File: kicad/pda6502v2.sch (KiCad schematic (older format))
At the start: 4 parts, among them U1 W65C02SxP, U2 AS6C62256-55PCN, U3 W65C22SxP, U4 AS6C62256-55PCN

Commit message: Lots of progress on schematic, some PCB part placement.
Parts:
- removed U3: W65C22SxP, Package_DIP:DIP-40_W15.24mm, symbol 65xx:W65C22SxP
- added C1, C10, C11, C14, C15, C16, C17, C2, C22, C23, C24, C3, C4, C5, C6, C7, C8, C9: 0.1μF, Capacitor_SMD:C_0805_2012Metric_Pad1.18x1.45mm_HandSolder, symbol Device:C_Small
- added C12: 100uF, Capacitor_THT:CP_Radial_D5.0mm_P2.00mm, symbol Device:CP
- added C13: 10uF, Capacitor_THT:CP_Radial_D5.0mm_P2.00mm, symbol Device:CP
- added C18, C19: 10nF, Capacitor_SMD:C_0805_2012Metric_Pad1.18x1.45mm_HandSolder, symbol Device:C_Small
- added C20, C21: 10uF, Capacitor_SMD:C_0805_2012Metric_Pad1.18x1.45mm_HandSolder, symbol Device:C_Small
- added D1: 1N5819, Diode_THT:D_DO-41_SOD81_P10.16mm_Horizontal, symbol Diode:1N5819
- added D10, D3, D4, D5, D6, D7, D8, D9: LED, LED_SMD:LED_0805_2012Metric_Pad1.15x1.40mm_HandSolder, symbol Device:LED_Small
- added D2: LED, LED_THT:LED_D3.0mm, symbol Device:LED
- added D?: 1N4148W, Diode_SMD:D_SOD-123, symbol Diode:1N4148W
- added J1: GPIOA, Connector_PinHeader_2.54mm:PinHeader_2x07_P2.54mm_Vertical, symbol Connector_Generic:Conn_02x07_Odd_Even
- added J2: GPIOB, Connector_PinHeader_2.54mm:PinHeader_2x07_P2.54mm_Vertical, symbol Connector_Generic:Conn_02x07_Odd_Even
- added J3: UART, Connector_PinHeader_2.54mm:PinHeader_2x06_P2.54mm_Vertical, symbol Connector_Generic:Conn_02x06_Odd_Even
- added J4: Screw_Terminal_01x02, TerminalBlock_Phoenix:TerminalBlock_Phoenix_MPT-0,5-2-2.54_1x02_P2.54mm_Horizontal, symbol Connector:Screw_Terminal_01x02
- added J5: Conn_01x02, Connector_PinHeader_2.54mm:PinHeader_1x02_P2.54mm_Vertical, symbol Connector_Generic:Conn_01x02
- added J6: PMOD A, Connector_PinSocket_2.54mm:PinSocket_2x06_P2.54mm_Horizontal, symbol Connector_Generic:Conn_02x06_Top_Bottom
- added J7: PMOD B, Connector_PinSocket_2.54mm:PinSocket_2x06_P2.54mm_Horizontal, symbol Connector_Generic:Conn_02x06_Top_Bottom
- added J?: ICSP, symbol Connector_Generic:Conn_02x03_Odd_Even
- added JP1: Jumper, Connector_PinHeader_2.54mm:PinHeader_1x02_P2.54mm_Vertical, symbol Device:Jumper
- added R1, R2, R21, R22, R23, R3, R4: 10K, Resistor_SMD:R_0805_2012Metric_Pad1.20x1.40mm_HandSolder, symbol Device:R_US
- added R24, R25, R26, R27: ?, Resistor_SMD:R_0805_2012Metric_Pad1.20x1.40mm_HandSolder, symbol Device:R_Small_US
- added R28, R29, R30, R31, R32, R33, R34, R35, R36: 1K, Resistor_SMD:R_0805_2012Metric_Pad1.20x1.40mm_HandSolder, symbol Device:R_Small_US
- added SW1: SW_Push, Button_Switch_THT:SW_Tactile_Straight_KSA0Axx1LFTR, symbol Switch:SW_Push
- added U10: LT3030, Package_SO:HTSSOP-20-1EP_4.4x6.5mm_P0.65mm_EP2.85x4mm, symbol pda6502v2:LT3030
- added U2: W65C22SxP, Package_DIP:DIP-40_W15.24mm, symbol 65xx:W65C22SxP
- added U3: SC28L92A1B, Package_QFP:PQFP-44_10x10mm_P0.8mm, symbol pda6502v2:SC28L92A1B
- added U4: DS1818, Package_TO_SOT_SMD:SOT-23_Handsoldering, symbol pda6502v2:DS1818
- added U7: AT25M01, Package_SO:SOIC-8_3.9x4.9mm_P1.27mm, symbol pda6502v2:AT25M01
- added U8: ICE40HX4K-TQ144, Package_QFP:TQFP-144_20x20mm_P0.5mm, symbol pda6502v2:ICE40HX4K-TQ144
- added U9: LM1117-3.3, Package_TO_SOT_THT:TO-220-3_Horizontal_TabDown, symbol Regulator_Linear:LM1117-3.3
- added X1: 3.6864 MHz, Oscillator:Oscillator_DIP-8, symbol Oscillator:CXO_DIP8
- added X2: 10 MHz, Oscillator:Oscillator_DIP-8, symbol Oscillator:CXO_DIP8
- U5: renamed from U4; value AS6C62256-55PCN -> AS6C4008-55PCN; footprint Package_DIP:DIP-28_W15.24mm -> Package_DIP:DIP-32_W15.24mm; symbol pda6502v2:AS6C62256-55PCN -> pda6502v2:AS6C4008-55PCN
- U6: renamed from U2; value AS6C62256-55PCN -> AS6C4008-55PCN; footprint Package_DIP:DIP-28_W15.24mm -> Package_DIP:DIP-32_W15.24mm; symbol pda6502v2:AS6C62256-55PCN -> pda6502v2:AS6C4008-55PCN
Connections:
- net labels added: +1V2, +2V5, +5V, A0, A1, A10, A11, A12, A13, A14, A15, A16, A17, A18, A2, A3, A4, A5, A6, A7, A8, A9, A[0..15], A[0..18], A[0..3], BLINKEN0, BLINKEN1, BLINKEN2, BLINKEN3, BLINKEN4, BLINKEN5, BLINKEN6, BLINKEN7, BLINKEN[0..7], BUSEN, CLOCK, CLOCKSRC, D0, D1, D2, D3, D4, D5, D6, D7, D[0..7], FLASH_MISO, FLASH_MOSI, FLASH_SCK, FLASH_~CS, PMODA0, PMODA1, PMODA2, PMODA3, PMODA4, PMODA5, PMODA6, PMODA7, PMODA[0..7], PMODB0, PMODB1, PMODB2, PMODB3, PMODB4, PMODB5, PMODB6, PMODB7, PMODB[0..7], PORTA_0, PORTA_1, PORTA_2, PORTA_3, PORTA_4, PORTA_5, PORTA_6, PORTA_7, PORTA_C1, PORTA_C2, PORTB_0, PORTB_1, PORTB_2, PORTB_3, PORTB_4, PORTB_5, PORTB_6, PORTB_7, PORTB_C1, PORTB_C2, READY, R~W, SYNC, UARTA_CTS, UARTA_RTS, UARTA_RX, UARTA_TX, UARTB_CTS, UARTB_RTS, UARTB_RX, UARTB_TX, UART_IM, UART_RXA~IRQ, UART_RXB~IRQ, UART_TXA~IRQ, UART_TXB~IRQ, UART_~CS, UART_~IRQ, UART_~RDN, UART_~WRN, VIA_~CS, VIA_~IRQ, ~IRQ, ~MLOCK, ~NMIRQ, ~RESET, ~SETOV, ~VECPULL
- net labels removed: ADDR0, ADDR1, ADDR10, ADDR11, ADDR12, ADDR13, ADDR14, ADDR15, ADDR2, ADDR3, ADDR4, ADDR5, ADDR6, ADDR7, ADDR8, ADDR9, ADDR[0..14], ADDR[0..15], ADDR[0..3], CLK, DATA0, DATA1, DATA2, DATA3, DATA4, DATA5, DATA6, DATA7, DATA[0..7], RWB
- wire segments 96 -> 494
- no-connect marks 2 -> 27
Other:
- moved on the sheet: U1

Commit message: WIP: remove PMOD. SMD LDO. Layout updates.
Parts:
- removed J5: Conn_01x02, Connector_PinHeader_2.54mm:PinHeader_1x02_P2.54mm_Vertical, symbol Connector_Generic:Conn_01x02
- removed J6: PMOD A, Connector_PinSocket_2.54mm:PinSocket_2x06_P2.54mm_Horizontal, symbol Connector_Generic:Conn_02x06_Top_Bottom
- removed J7: PMOD B, Connector_PinSocket_2.54mm:PinSocket_2x06_P2.54mm_Horizontal, symbol Connector_Generic:Conn_02x06_Top_Bottom
- removed JP1: Jumper, Connector_PinHeader_2.54mm:PinHeader_1x02_P2.54mm_Vertical, symbol Device:Jumper
- removed U9: LM1117-3.3, Package_TO_SOT_THT:TO-220-3_Horizontal_TabDown, symbol Regulator_Linear:LM1117-3.3
- removed X1: 3.6864 MHz, Oscillator:Oscillator_DIP-8, symbol Oscillator:CXO_DIP8
- removed X2: 10 MHz, Oscillator:Oscillator_DIP-8, symbol Oscillator:CXO_DIP8
- added J5: Conn_02x04_Odd_Even, Connector_PinSocket_2.54mm:PinSocket_2x04_P2.54mm_Vertical, symbol Connector_Generic:Conn_02x04_Odd_Even
- added U9: TLV1117-33, Package_TO_SOT_SMD:SOT-223, symbol Regulator_Linear:TLV1117-33
- added X1: 10 MHz, Oscillator:Oscillator_SMD_EuroQuartz_XO53-4Pin_5.0x3.2mm, symbol pda6502v2:XO53
- added X2: 3.6864 MHz, Oscillator:Oscillator_SMD_EuroQuartz_XO53-4Pin_5.0x3.2mm, symbol pda6502v2:XO53
- J1, J2: footprint Connector_PinHeader_2.54mm:PinHeader_2x07_P2.54mm_Vertical -> Connector_PinSocket_2.54mm:PinSocket_2x07_P2.54mm_Vertical
- J6: renamed from J?; footprint (none) -> Connector_PinHeader_2.54mm:PinHeader_2x03_P2.54mm_Vertical
- gave numbers to parts that had none: 1
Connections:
- net labels removed: PMODA0, PMODA1, PMODA2, PMODA3, PMODA4, PMODA5, PMODA6, PMODA7, PMODA[0..7], PMODB0, PMODB1, PMODB2, PMODB3, PMODB4, PMODB5, PMODB6, PMODB7, PMODB[0..7]
- wire segments 494 -> 453
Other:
- moved on the sheet: C12, C13, D10, D2, D3, D4, D5, D6, D7, D8, D9, J4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

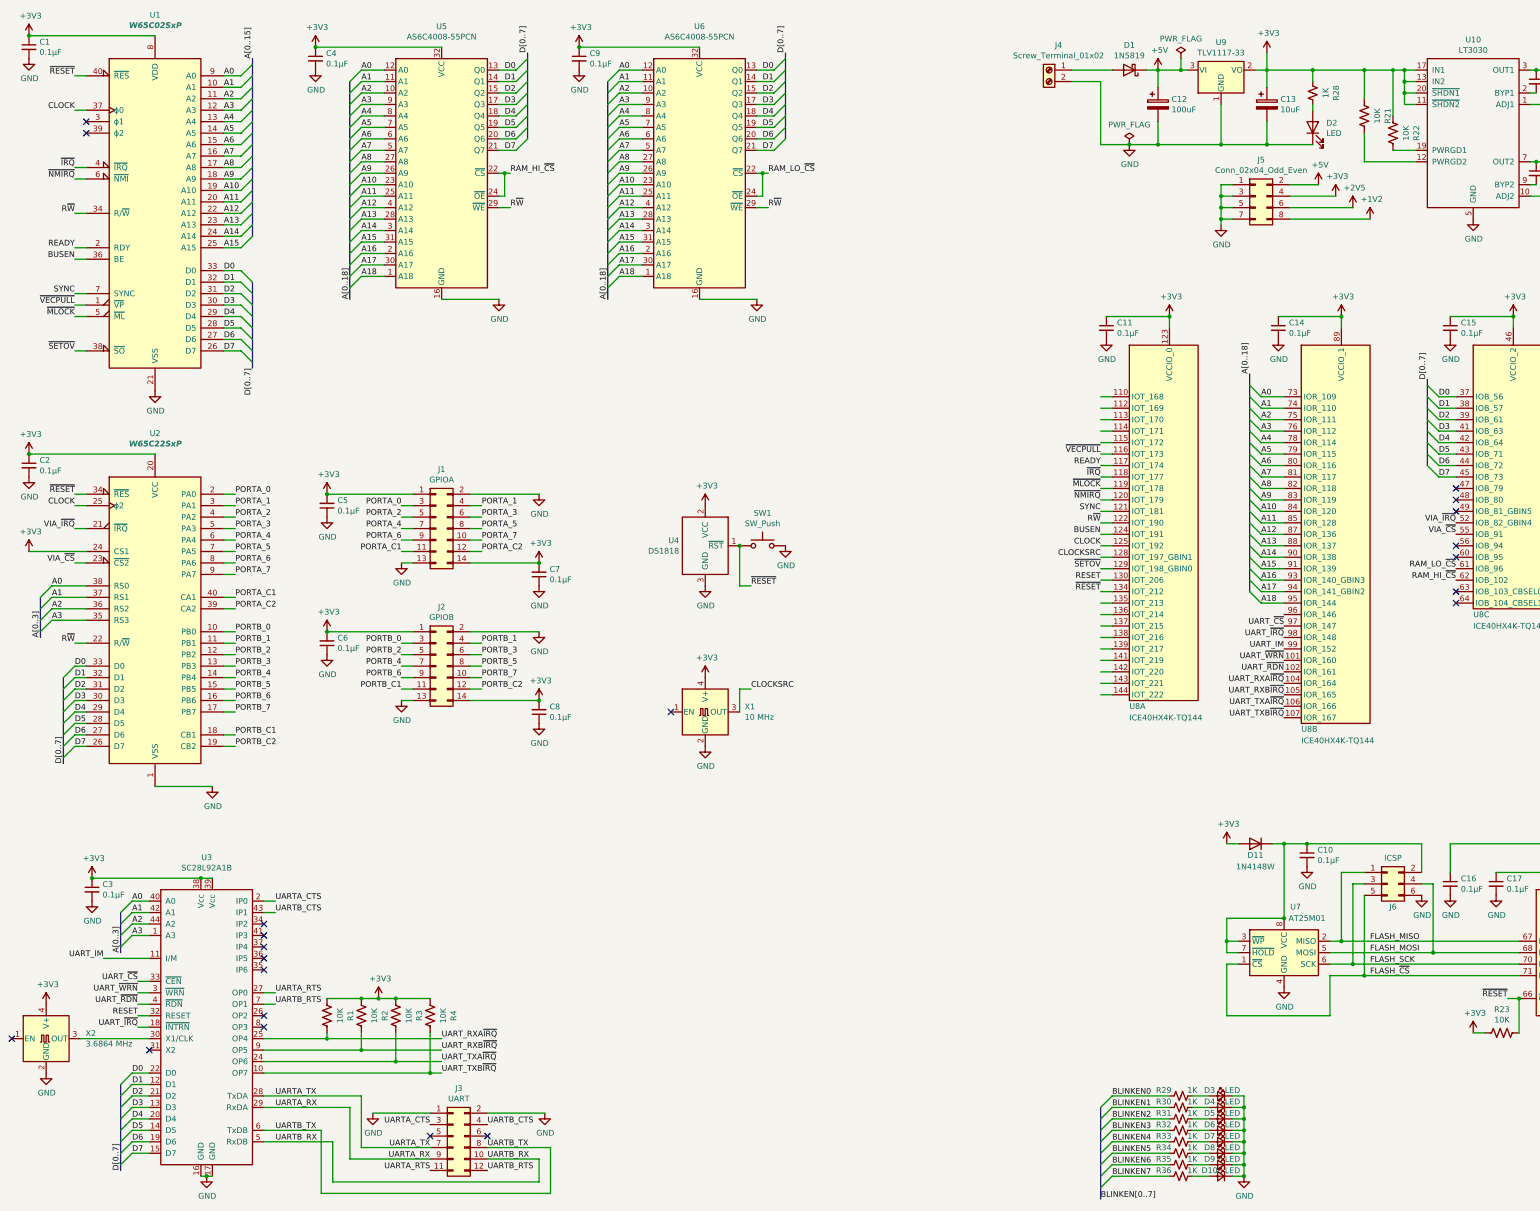
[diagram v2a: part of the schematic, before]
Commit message: Dual 6522 VIA; PCB layout progress.
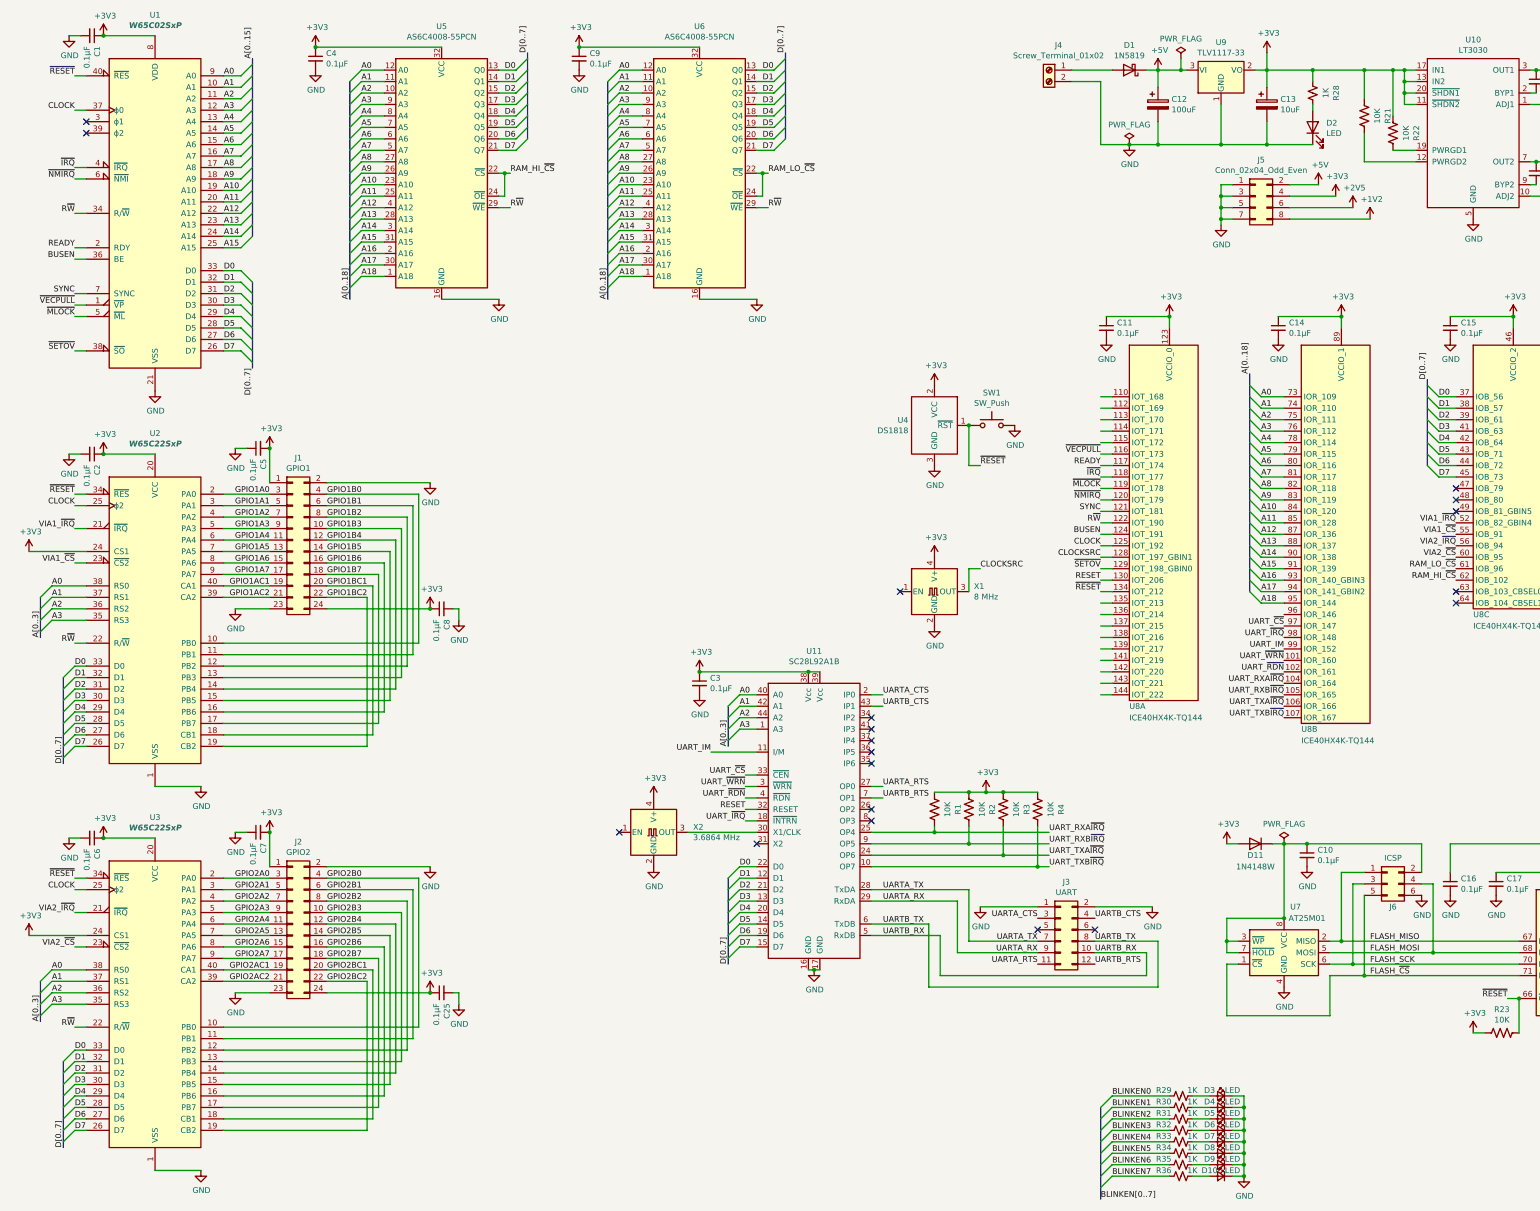
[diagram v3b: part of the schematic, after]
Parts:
- removed J1: GPIOA, Connector_PinSocket_2.54mm:PinSocket_2x07_P2.54mm_Vertical, symbol Connector_Generic:Conn_02x07_Odd_Even
- removed J2: GPIOB, Connector_PinSocket_2.54mm:PinSocket_2x07_P2.54mm_Vertical, symbol Connector_Generic:Conn_02x07_Odd_Even
- removed U2: W65C22SxP, Package_DIP:DIP-40_W15.24mm, symbol 65xx:W65C22SxP
- added C25: 0.1μF, Capacitor_SMD:C_0805_2012Metric_Pad1.18x1.45mm_HandSolder, symbol Device:C_Small
- added J1: GPIO1, Connector_PinSocket_2.54mm:PinSocket_2x12_P2.54mm_Vertical, symbol Connector_Generic:Conn_02x12_Odd_Even
- added J2: GPIO2, Connector_PinSocket_2.54mm:PinSocket_2x12_P2.54mm_Vertical, symbol Connector_Generic:Conn_02x12_Odd_Even
- added U2, U3: W65C22SxP, Package_DIP:DIP-40_W15.24mm, symbol pda6502v2:W65C22SxP
- X1: value 10 MHz -> 8 MHz
- renumbered U3 to U11
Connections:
- net +3V3: now also C6.1, C8.1, C25.1, J1.1 (Pin_1), J1.24 (Pin_24), J2.1 (Pin_1), J2.24 (Pin_24), U2.20 (VCC), U2.24 (CS1), U3.20 (VCC), U3.24 (CS1); no longer C6.2, C8.2
- net A0: now also U2.38 (RS0), U3.38 (RS0)
- net A1: now also U2.37 (RS1), U3.37 (RS1)
- net A2: now also U2.36 (RS2), U3.36 (RS2)
- net A3: now also U2.35 (RS3), U3.35 (RS3)
- net CLOCK: now also U2.25 (ϕ2), U3.25 (ϕ2)
- net D0: now also U2.33 (D0), U3.33 (D0)
- net D1: now also U2.32 (D1), U3.32 (D1)
- net D2: now also U2.31 (D2), U3.31 (D2)
- net D3: now also U2.30 (D3), U3.30 (D3)
- net D4: now also U2.29 (D4), U3.29 (D4)
- net D5: now also U2.28 (D5), U3.28 (D5)
- net D6: now also U2.27 (D6), U3.27 (D6)
- net D7: now also U2.26 (D7), U3.26 (D7)
- net GND: now also C6.2, C8.2, C25.2, J1.2 (Pin_2), J1.23 (Pin_23), J2.2 (Pin_2), J2.23 (Pin_23), U2.1 (VSS), U3.1 (VSS); no longer C6.1, C8.1
- net R~W: now also U2.22 (R/~W), U3.22 (R/~W)
- net ~RESET: now also U2.34 (~RES), U3.34 (~RES)
- net VIA2_~IRQ: now reaches U8.56 (IOB_94)
- net VIA2_~IRQ: now also U3.21 (~IRQ)
- net VIA2_~CS: now reaches U8.60 (IOB_95)
- net VIA2_~CS: now also U3.23 (~CS2)
- net VIA_~CS renamed VIA1_~CS
- net VIA1_~CS: now also U2.23 (~CS2)
- net VIA_~IRQ renamed VIA1_~IRQ
- net VIA1_~IRQ: now also U2.21 (~IRQ)
- new net GPIO1A0: J1.3 (Pin_3), U2.2 (PA0)
- new net GPIO1A1: J1.5 (Pin_5), U2.3 (PA1)
- new net GPIO1A2: J1.7 (Pin_7), U2.4 (PA2)
- new net GPIO1A3: J1.9 (Pin_9), U2.5 (PA3)
- new net GPIO1A4: J1.11 (Pin_11), U2.6 (PA4)
- new net GPIO1A5: J1.13 (Pin_13), U2.7 (PA5)
- new net GPIO1A6: J1.15 (Pin_15), U2.8 (PA6)
- new net GPIO1A7: J1.17 (Pin_17), U2.9 (PA7)
- new net GPIO1AC1: J1.19 (Pin_19), U2.40 (CA1)
- new net GPIO1AC2: J1.21 (Pin_21), U2.39 (CA2)
- new net GPIO1B0: J1.4 (Pin_4), U2.10 (PB0)
- new net GPIO1B1: J1.6 (Pin_6), U2.11 (PB1)
- new net GPIO1B2: J1.8 (Pin_8), U2.12 (PB2)
- new net GPIO1B3: J1.10 (Pin_10), U2.13 (PB3)
- new net GPIO1B4: J1.12 (Pin_12), U2.14 (PB4)
- new net GPIO1B5: J1.14 (Pin_14), U2.15 (PB5)
- new net GPIO1B6: J1.16 (Pin_16), U2.16 (PB6)
- new net GPIO1B7: J1.18 (Pin_18), U2.17 (PB7)
- new net GPIO1BC1: J1.20 (Pin_20), U2.18 (CB1)
- new net GPIO1BC2: J1.22 (Pin_22), U2.19 (CB2)
- new net GPIO2A0: J2.3 (Pin_3), U3.2 (PA0)
- new net GPIO2A1: J2.5 (Pin_5), U3.3 (PA1)
- new net GPIO2A2: J2.7 (Pin_7), U3.4 (PA2)
- new net GPIO2A3: J2.9 (Pin_9), U3.5 (PA3)
- new net GPIO2A4: J2.11 (Pin_11), U3.6 (PA4)
- new net GPIO2A5: J2.13 (Pin_13), U3.7 (PA5)
- new net GPIO2A6: J2.15 (Pin_15), U3.8 (PA6)
- new net GPIO2A7: J2.17 (Pin_17), U3.9 (PA7)
- new net GPIO2AC1: J2.19 (Pin_19), U3.40 (CA1)
- new net GPIO2AC2: J2.21 (Pin_21), U3.39 (CA2)
- new net GPIO2B0: J2.4 (Pin_4), U3.10 (PB0)
- new net GPIO2B1: J2.6 (Pin_6), U3.11 (PB1)
- new net GPIO2B2: J2.8 (Pin_8), U3.12 (PB2)
- new net GPIO2B3: J2.10 (Pin_10), U3.13 (PB3)
- new net GPIO2B4: J2.12 (Pin_12), U3.14 (PB4)
- new net GPIO2B5: J2.14 (Pin_14), U3.15 (PB5)
- new net GPIO2B6: J2.16 (Pin_16), U3.16 (PB6)
- new net GPIO2B7: J2.18 (Pin_18), U3.17 (PB7)
- new net GPIO2BC1: J2.20 (Pin_20), U3.18 (CB1)
- new net GPIO2BC2: J2.22 (Pin_22), U3.19 (CB2)
- no-connect marks 27 -> 25
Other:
- moved on the sheet: C1, C2, C3, C5, C8, J3, R1, R2, R3, R4, SW1, U11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
